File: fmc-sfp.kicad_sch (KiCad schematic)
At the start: 41 parts, among them J1 ASP-134604-01, J2 SFP+, J3 SFP+, J4 132134, J5 132134, J6 132134, J7 132134, U1 MAX9113EKA_TT, U2 MAX9113EKA_TT

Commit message: update after Phil review
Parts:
- removed J2, J3: SFP+, Connector:Connector_SFP_and_Cage, symbol Interface_Optical:SFP+
- removed R10, R15, R16, R17, R18, R7, R8, R9: 10k, Resistor_SMD:R_0603_1608Metric, symbol Device:R_US
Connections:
- no-connect marks 160 -> 134
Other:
- added sheet SPF0 (SFP.kicad_sch)
- added sheet SPF1 (SFP.kicad_sch)

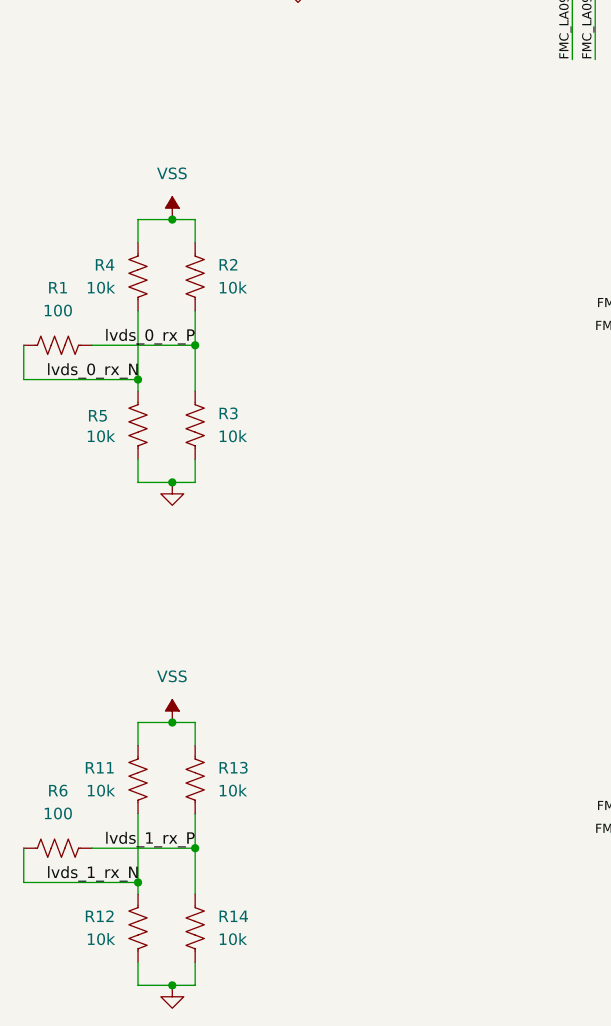
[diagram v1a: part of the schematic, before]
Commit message: move termination resistors to FPGA side of capacitors
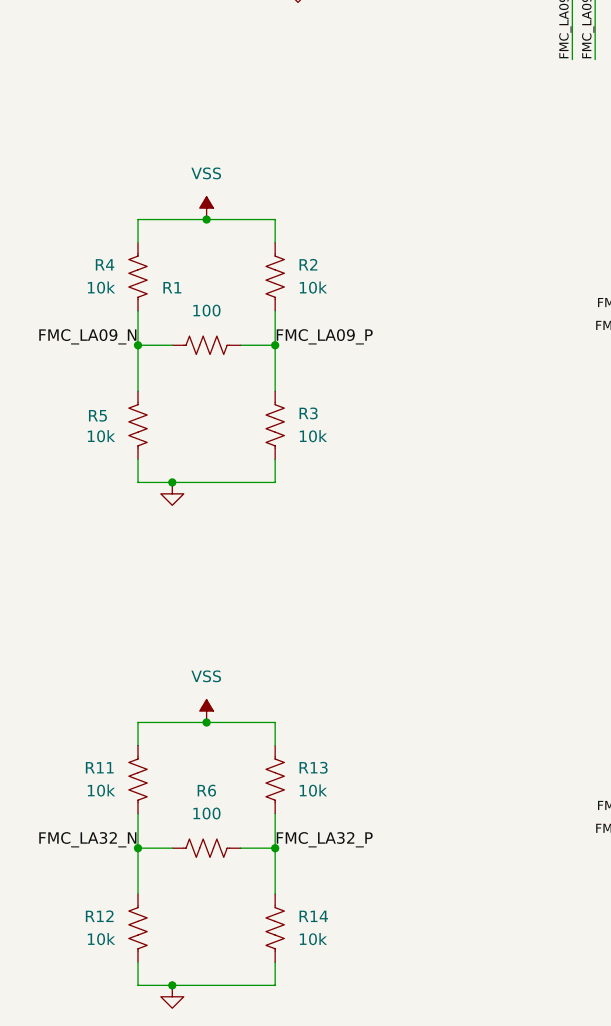
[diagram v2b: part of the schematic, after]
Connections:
- net FMC_LA09_N: now also R1.1, R4.2, R5.1
- net FMC_LA09_P: now also R1.2, R2.2, R3.1
- net FMC_LA32_N: now also R11.2, R12.1, R6.1
- net FMC_LA32_P: now also R13.2, R14.1, R6.2
- net lvds_0_rx_N: no longer R1.1, R4.2, R5.1
- net lvds_0_rx_P: no longer R1.2, R2.2, R3.1
- net lvds_1_rx_N: no longer R11.2, R12.1, R6.1
- net lvds_1_rx_P: no longer R13.2, R14.1, R6.2
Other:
- moved on the sheet: R1, R13, R14, R2, R3, R6

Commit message: update capacitor part numbers
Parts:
- C10, C12: MANUFACTURER Aillen -> KEMET; MPN 0603B102K500SD -> C0603C102K5RAC7867
- C11, C9: MANUFACTURER Aillen -> KEMET; MPN 0603B104K500XD -> C0603C104M5RAC7867
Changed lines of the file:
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@@
 			)
 		)
-		(property "MANUFACTURER" "Aillen"
+		(property "MANUFACTURER" "KEMET"
 			(at 196.85 139.7 0)
 			(effects
@@
 			)
 		)
-		(property "MPN" "0603B104K500XD"
+		(property "MPN" "C0603C104M5RAC7867"
 			(at 196.85 139.7 0)
 			(effects
@@
 			)
 		)
-		(property "MANUFACTURER" "Aillen"
+		(property "MANUFACTURER" "KEMET"
 			(at 212.09 93.98 0)
 			(effects
@@
 			)
 		)
-		(property "MPN" "0603B102K500SD"
+		(property "MPN" "C0603C102K5RAC7867"
 			(at 212.09 93.98 0)
 			(effects
@@
 			)
 		)
-		(property "MANUFACTURER" "Aillen"
+		(property "MANUFACTURER" "KEMET"
 			(at 200.66 93.98 0)
 			(effects
@@
 			)
 		)
-		(property "MPN" "0603B104K500XD"
+		(property "MPN" "C0603C104M5RAC7867"
 			(at 200.66 93.98 0)
 			(effects
@@
 			)
 		)
-		(property "MANUFACTURER" "Aillen"
+		(property "MANUFACTURER" "KEMET"
 			(at 208.28 139.7 0)
 			(effects
@@
 			)
 		)
-		(property "MPN" "0603B102K500SD"
+		(property "MPN" "C0603C102K5RAC7867"
 			(at 208.28 139.7 0)
 			(effects

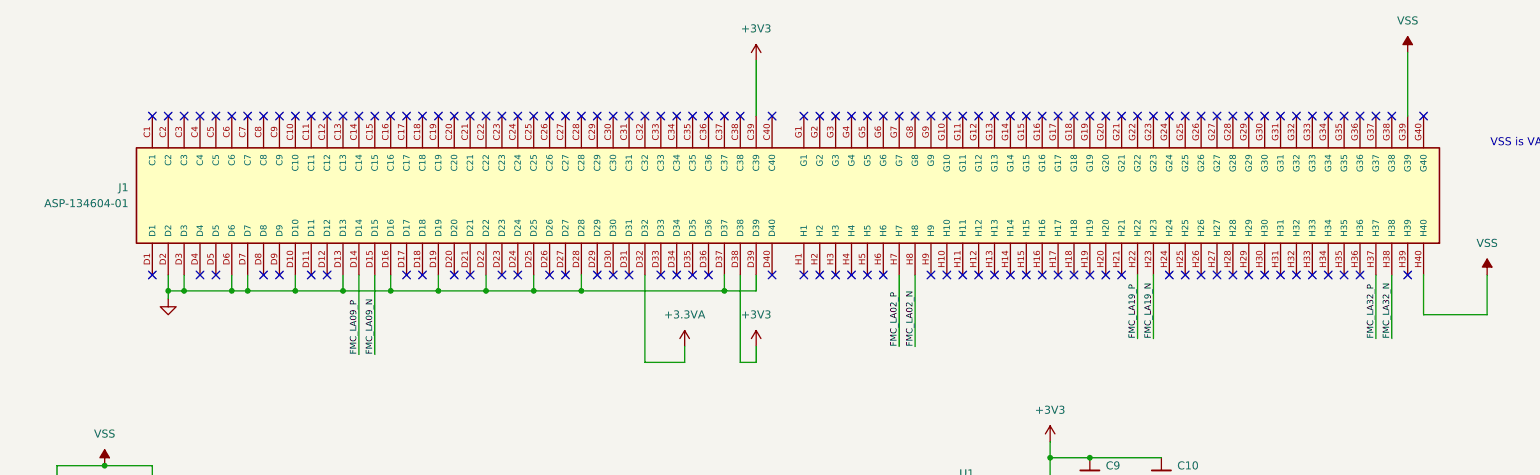
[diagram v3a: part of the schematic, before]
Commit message: connect all grounds for fmc connector
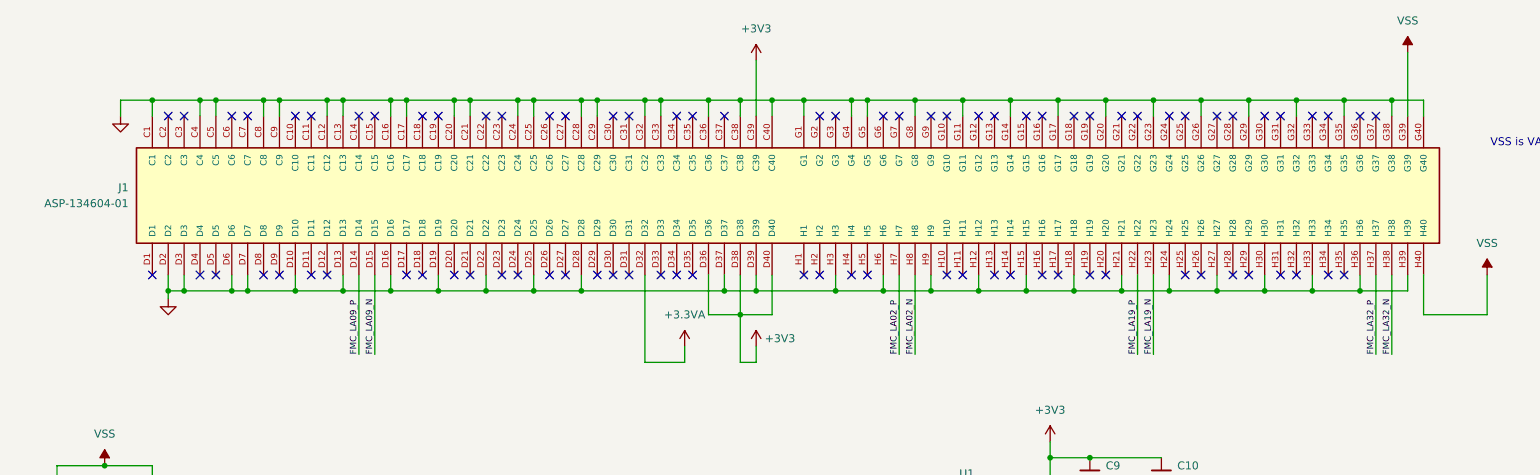
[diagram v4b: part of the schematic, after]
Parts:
- J1: footprint ASP_134604_01:SAMTEC_ASP-134604-01 -> project:SAMTEC_ASP-134604-01
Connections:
- net +3V3: now also J1.D36, J1.D40
- net GND: now also J1.C1, J1.C12, J1.C13, J1.C16, J1.C17, J1.C20, J1.C21, J1.C24, J1.C25, J1.C28, J1.C29, J1.C32, J1.C33, J1.C36, J1.C38, J1.C4, J1.C40, J1.C5, J1.C8, J1.C9, J1.G1, J1.G11, J1.G14, J1.G17, J1.G20, J1.G23, J1.G26, J1.G29, J1.G32, J1.G35, J1.G38, J1.G4, J1.G40, J1.G5, J1.G8, J1.H12, J1.H15, J1.H18, J1.H21, J1.H24, J1.H27, J1.H3, J1.H30, J1.H33, J1.H36, J1.H39, J1.H6, J1.H9
- no-connect marks 134 -> 84

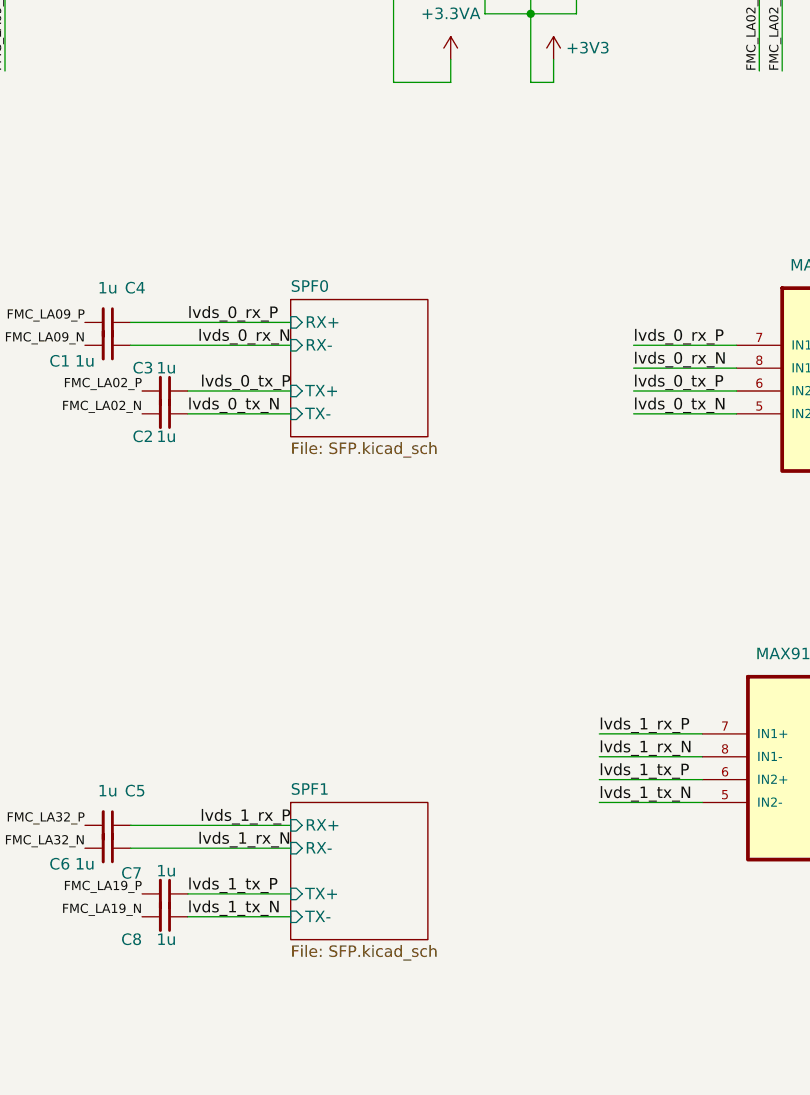
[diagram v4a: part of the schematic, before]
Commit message: update sfp footprint, add git commit to silkscreen
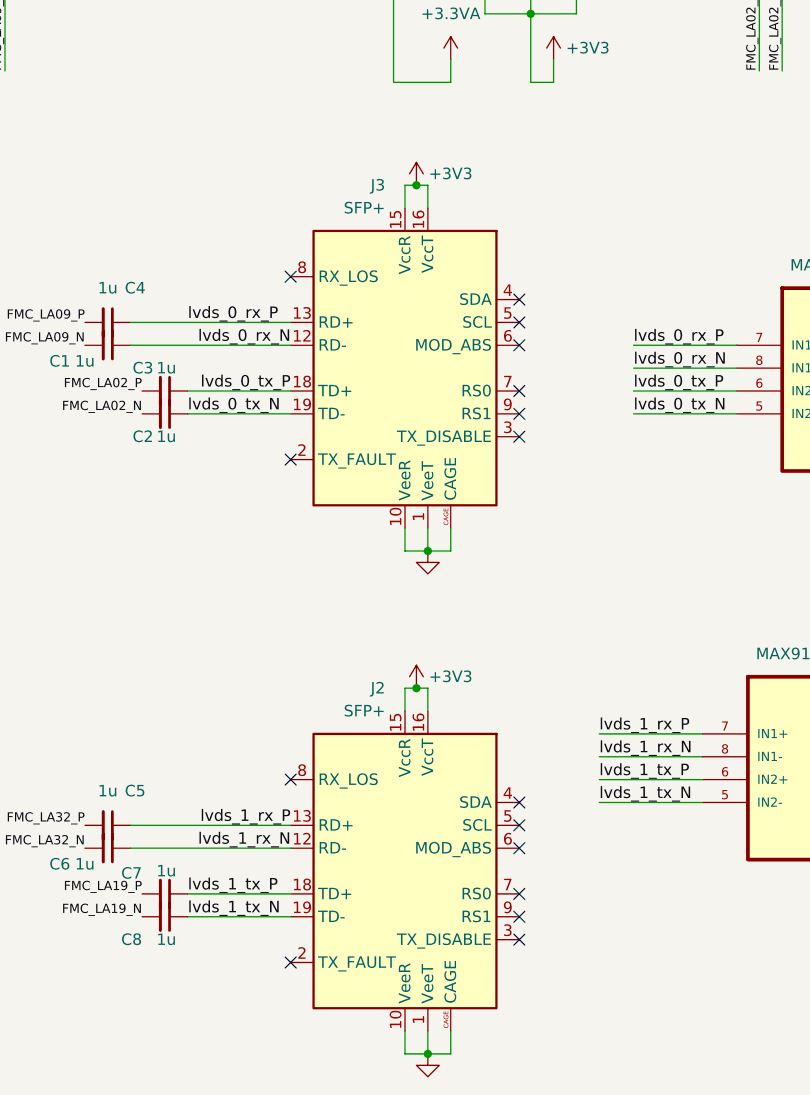
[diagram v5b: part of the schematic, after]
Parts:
- added J2, J3: SFP+, project:SFP_and_Cage, symbol Interface_Optical:SFP+
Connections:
- net +3V3: now also J2.15 (VccR), J2.16 (VccT), J3.15 (VccR), J3.16 (VccT)
- net GND: now also J2.1 (VeeT), J2.10 (VeeR), J2.11 (VeeR), J2.14 (VeeR), J2.17 (VeeT), J2.20 (VeeT), J2.CAGE, J3.1 (VeeT), J3.10 (VeeR), J3.11 (VeeR), J3.14 (VeeR), J3.17 (VeeT), J3.20 (VeeT), J3.CAGE
- net lvds_0_rx_N: now also J3.12 (RD-)
- net lvds_0_rx_P: now also J3.13 (RD+)
- net lvds_0_tx_N: now also J3.19 (TD-)
- net lvds_0_tx_P: now also J3.18 (TD+)
- net lvds_1_rx_N: now also J2.12 (RD-)
- net lvds_1_rx_P: now also J2.13 (RD+)
- net lvds_1_tx_N: now also J2.19 (TD-)
- net lvds_1_tx_P: now also J2.18 (TD+)
- no-connect marks 84 -> 100
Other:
- removed sheet SPF0
- removed sheet SPF1

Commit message: set part number for sfp cage
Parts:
- J2, J3: MANUFACTURER (none) -> SAMTEC; MPN (none) -> SFPK-SL

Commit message: modify title block
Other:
- company: (none) -> MicroRidge Technology LTD
- title: (none) -> FMC-SFP
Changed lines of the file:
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@@
 	(generator_version "8.0")
 	(paper "A4")
+	(title_block
+		(title "FMC-SFP")
+		(date "2024-05-08")
+		(rev "Rev0")
+		(company "MicroRidge Technology LTD")
+	)
 	(junction
 		(at 205.74 64.77)

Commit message: Change resistors to 0805, add switch to disable DC Bias
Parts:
- removed C1, C2, C3, C4, C5, C6, C7, C8: 1u, Capacitor_SMD:C_0603_1608Metric, symbol Device:C_Small
- added R10, R15, R16, R17, R18, R7, R8, R9: 0, Resistor_SMD:R_0805_2012Metric_Pad1.20x1.40mm_HandSolder, symbol Device:R_Small_US
- added SW1: CHS-02TB, Button_Switch_SMD:SW_DIP_SPSTx02_Slide_Copal_CHS-02B_W7.62mm_P1.27mm, symbol Switch:SW_DIP_x02
- R1, R6: footprint Resistor_SMD:R_0603_1608Metric -> Resistor_SMD:R_0805_2012Metric_Pad1.20x1.40mm_HandSolder; MANUFACTURER YAGEO -> UNI-ROYAL(Uniroyal Elec); MPN RC0402FR-07100KL -> 0805W8F1000T5E
- R11, R12, R13, R14, R2, R3, R4, R5: footprint Resistor_SMD:R_0603_1608Metric -> Resistor_SMD:R_0805_2012Metric_Pad1.20x1.40mm_HandSolder; MANUFACTURER Bourns Inc. -> UNI-ROYAL(Uniroyal Elec); MPN CR0603-FX-1002ELF -> 0805W8F1002T5E
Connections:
- net FMC_LA02_N: now also R10.1
- net FMC_LA02_P: now also R9.1
- net FMC_LA09_N: now also R8.1
- net FMC_LA09_P: now also R7.1
- net FMC_LA19_N: now also R18.1
- net FMC_LA19_P: now also R17.1
- net FMC_LA32_N: now also R16.1
- net FMC_LA32_P: now also R15.1
- net GND: now also SW1.1; no longer R12.2, R14.2, R3.2, R5.2
- net VSS: no longer J1.G39, J1.H40, R11.1, R13.1, R2.1, R4.1
- net lvds_0_rx_N: now also R8.2
- net lvds_0_rx_P: now also R7.2
- net lvds_0_tx_N: now also R10.2
- net lvds_0_tx_P: now also R9.2
- net lvds_1_rx_N: now also R16.2
- net lvds_1_rx_P: now also R15.2
- net lvds_1_tx_N: now also R18.2
- net lvds_1_tx_P: now also R17.2
- new net VADJ: J1.G39, J1.H40, SW1.2
- new net bias_hi: R11.1, R13.1, R2.1, R4.1, SW1.3
- new net bias_lo: R12.2, R14.2, R3.2, R5.2, SW1.4
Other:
- note removed: "VSS is VADJ"
